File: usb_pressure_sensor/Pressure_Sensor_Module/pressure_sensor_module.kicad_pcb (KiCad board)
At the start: 2 copper layers, 3 parts, among them IC1 MS580314BA01-00, J1 MODULE_BRIDGE

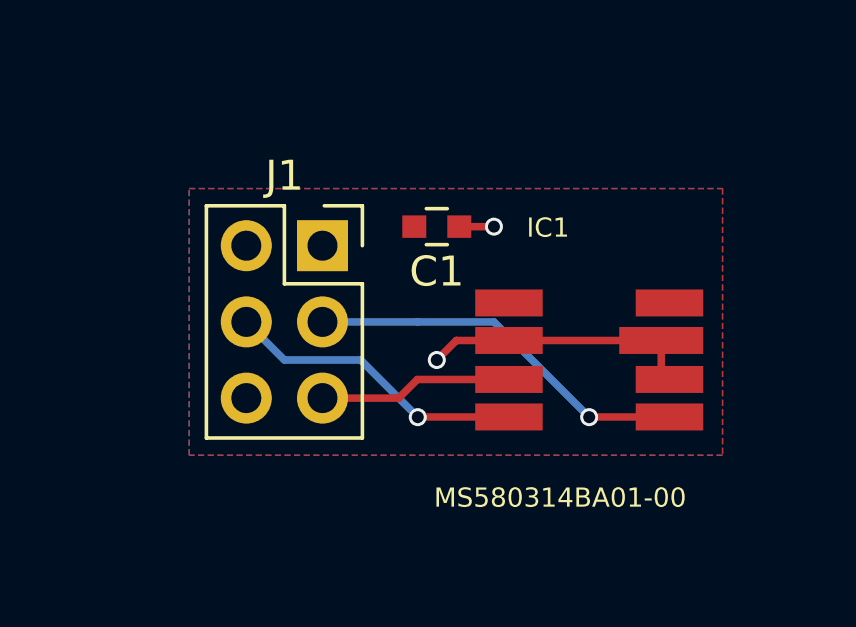
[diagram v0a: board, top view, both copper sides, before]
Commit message: PCB design with new pressure sensor and some footprints
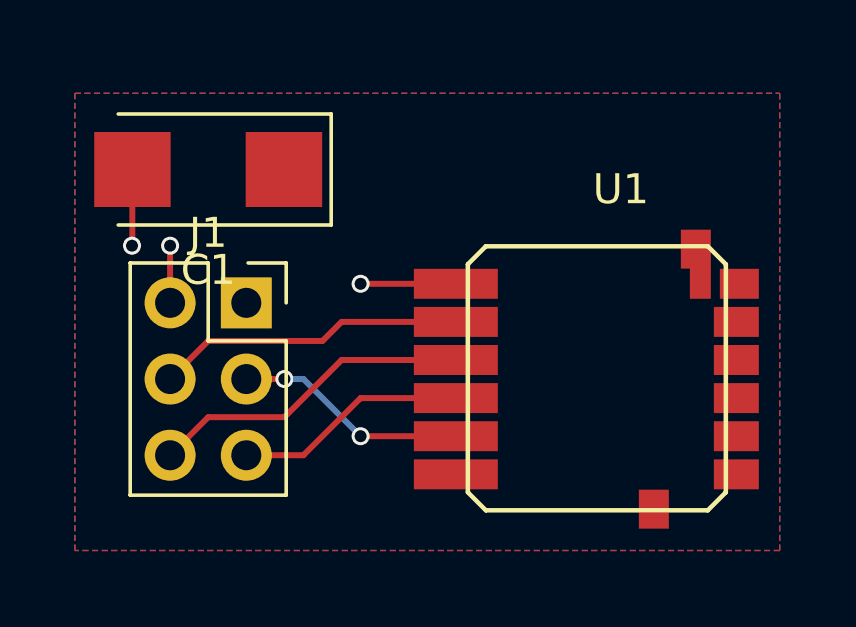
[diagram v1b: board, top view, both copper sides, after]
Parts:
- removed IC1: MS580314BA01-00, footprints:XDCR_MS580314BA01-00
- added U1: MS5535C, footprints:MS5535C, F.Cu at (144.1, 111.8)
- C1: value 100n -> 47u; footprint Capacitors_SMD:C_0603 -> Capacitors_Tantalum_SMD:CP_Tantalum_Case-C_EIA-6032-28_Reflow
- moved C1 7.85 mm to (135.9, 101.6)
- moved J1 3.17 mm to (137.2, 106.0)
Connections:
- C1 pad 1: /GND -> /3v3
- C1 pad 2: /VCC -> /GND
- J1 pad 1: /GND -> /3v3
- J1 pad 2: /VCC -> /GND
- J1 pad 3: /SPI_SCLK -> /MCLK
- J1 pad 4: /SPI_MISO -> /SCLK
- J1 pad 5: /SPI_MOSI -> /DIN
- J1 pad 6: Net-(J1-Pad6) -> /DOUT
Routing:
- net /SPI_SCLK: track 12.9 -> 0.00 mm, vias 1 -> 0
- net /DOUT: track 0.00 -> 10.8 mm
- net /SCLK: track 0.00 -> 10.3 mm
- net /SPI_MISO: track 10.1 -> 0.00 mm, vias 1 -> 0
- net /MCLK: track 0.00 -> 7.77 mm, vias 0 -> 2
- net /DIN: track 0.00 -> 7.77 mm
- net /SPI_MOSI: track 6.47 -> 0.00 mm
- net /GND: track 10.3 -> 7.63 mm, vias 2 -> 3
- added copper zone on F.Cu, net /3v3
- removed copper zone on F.Cu, net /VCC
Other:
- net class Default: trace_width 0.25 -> 0.2
- rule pad_to_mask_clearance: 0.2 -> 0

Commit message: added cuts and drills + logos into the PCBs
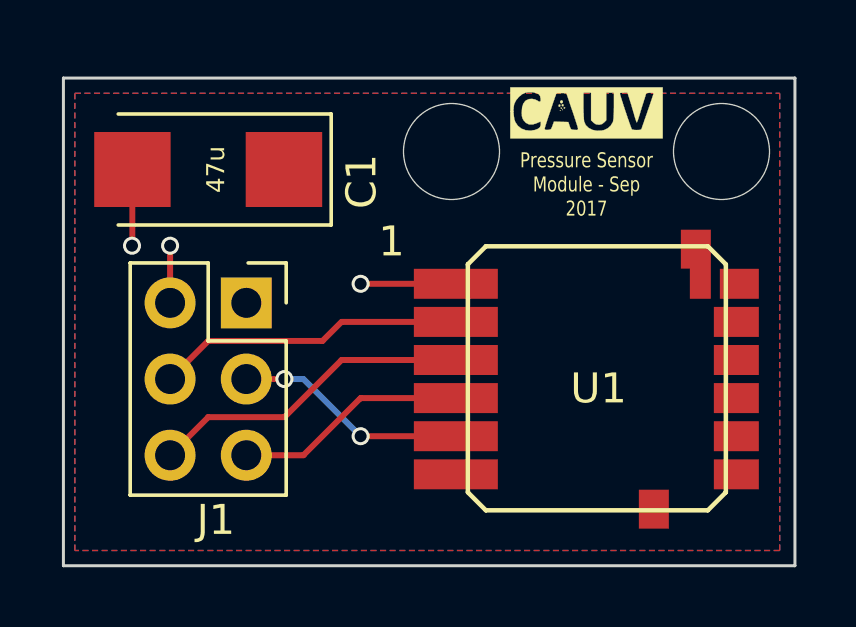
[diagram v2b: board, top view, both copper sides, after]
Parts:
- added G***: LOGO, footprints:LOGO, F.Cu at (148.5, 99.7)
- added REF**: M3_HOLE, agg:M3_HOLE, F.Cu at (144.0, 101.0)
- added REF**: M3_HOLE, agg:M3_HOLE, F.Cu at (153.0, 101.0)
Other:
- board outline added: 24.4 x 16.3 mm
- board text added: "1"
- board text added: "47u"
- board text added: "Pressure Sensor Module - Sep 2017"

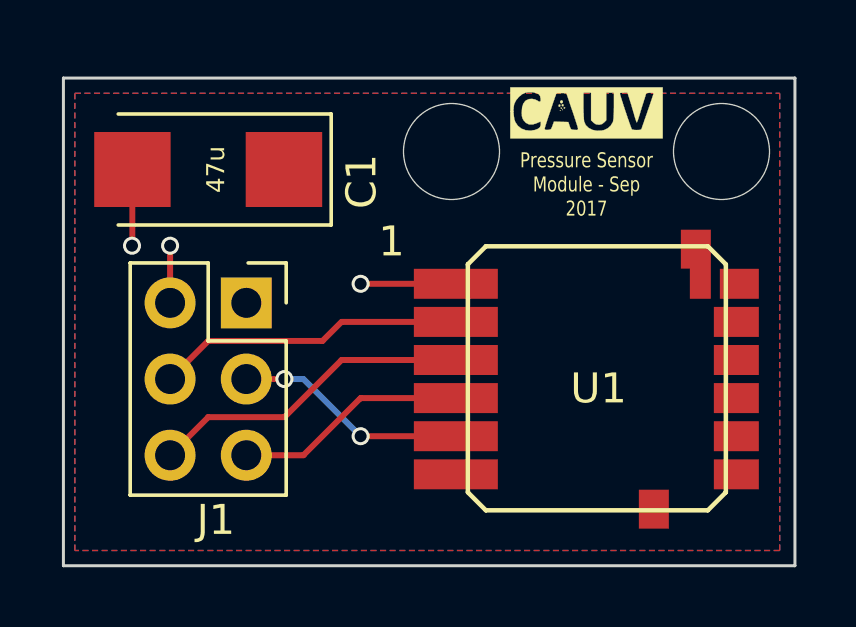
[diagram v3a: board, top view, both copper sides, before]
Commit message: removed unnecessary via
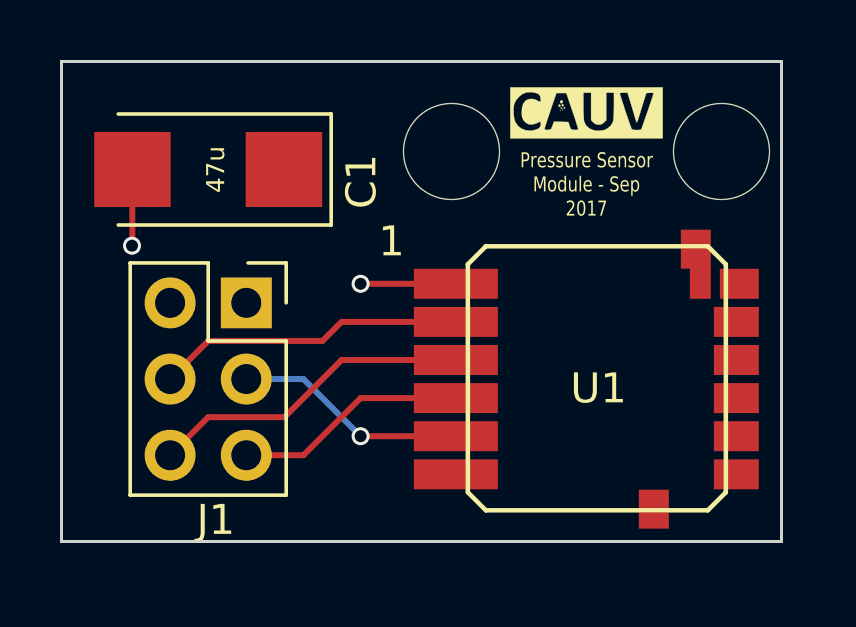
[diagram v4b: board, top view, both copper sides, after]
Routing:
- net /GND: track 7.63 -> 5.72 mm, vias 3 -> 2
- net /MCLK: vias 2 -> 1
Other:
- board size 24.4 x 16.3 mm -> 24 x 16 mm
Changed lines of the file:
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@@
     (thickness 1.6)
     (drawings 7)
-    (tracks 24)
+    (tracks 20)
     (zones 0)
     (modules 6)
@@
   (page A4)
   (layers
-    (0 F.Cu signal hide)
-    (31 B.Cu signal hide)
+    (0 F.Cu signal)
+    (31 B.Cu signal)
     (32 B.Adhes user hide)
     (33 F.Adhes user hide)
@@
     (pad "" np_thru_hole circle (at 0 0) (size 3.2 3.2) (drill 3.2) (layers *.Cu F.Mask))
   )
+  (module agg:M3_HOLE (layer F.Cu)
+    (at 153 101)
+    (fp_text reference REF** (at 0 -2.5) (layer F.Fab) hide
+      (effects (font (size 1 1) (thickness 0.15)))
+    )
+    (fp_text value M3_HOLE (at 0 2.5) (layer F.Fab) hide
+      (effects (font (size 1 1) (thickness 0.15)))
+    )
+    (fp_line (start -1.8 1.8) (end -1.8 -1.8) (layer F.CrtYd) (width 0.01))
+    (fp_line (start 1.8 1.8) (end -1.8 1.8) (layer F.CrtYd) (width 0.01))
+    (fp_line (start 1.8 -1.8) (end 1.8 1.8) (layer F.CrtYd) (width 0.01))
+    (fp_line (start -1.8 -1.8) (end 1.8 -1.8) (layer F.CrtYd) (width 0.01))
+    (pad "" np_thru_hole circle (at 0 0) (size 3.2 3.2) (drill 3.2) (layers *.Cu F.Mask))
+  )
   (module Capacitors_Tantalum_SMD:CP_Tantalum_Case-C_EIA-6032-28_Reflow (layer F.Cu)
     (at 135.89 101.6 180)
@@
     (pad 14 smd rect (at -8.15 6.3525 180) (size 0.7 1.005) (layers F.Cu F.Paste F.Mask))
     (pad 14 smd rect (at -8 7.505 180) (size 1 1.3) (layers F.Cu F.Paste F.Mask))
-  )
-  (module agg:M3_HOLE (layer F.Cu)
-    (at 153 101)
-    (fp_text reference REF** (at 0 -2.5) (layer F.Fab) hide
-      (effects (font (size 1 1) (thickness 0.15)))
-    )
-    (fp_text value M3_HOLE (at 0 2.5) (layer F.Fab) hide
-      (effects (font (size 1 1) (thickness 0.15)))
-    )
-    (fp_line (start -1.8 1.8) (end -1.8 -1.8) (layer F.CrtYd) (width 0.01))
-    (fp_line (start 1.8 1.8) (end -1.8 1.8) (layer F.CrtYd) (width 0.01))
-    (fp_line (start 1.8 -1.8) (end 1.8 1.8) (layer F.CrtYd) (width 0.01))
-    (fp_line (start -1.8 -1.8) (end 1.8 -1.8) (layer F.CrtYd) (width 0.01))
-    (pad "" np_thru_hole circle (at 0 0) (size 3.2 3.2) (drill 3.2) (layers *.Cu F.Mask))
   )
   (module footprints:LOGO (layer F.Cu)
@@
       (xy -0.794329 -0.385252)) (layer F.SilkS) (width 0.01))
   )
+  (gr_line (start 155 98) (end 155 114) (layer Edge.Cuts) (width 0.1))
+  (gr_line (start 131 98) (end 155 98) (layer Edge.Cuts) (width 0.1))
+  (gr_line (start 131 114) (end 131 98) (layer Edge.Cuts) (width 0.1))
+  (gr_line (start 155 114) (end 131 114) (layer Edge.Cuts) (width 0.1))
   (gr_text "Pressure Sensor\nModule - Sep\n2017" (at 148.5 102.1) (layer F.SilkS)
     (effects (font (size 0.5 0.4) (thickness 0.1)))
@@
     (effects (font (size 0.6 0.6) (thickness 0.15)))
   )
-  (gr_line (start 155.448 98.552) (end 131.064 98.552) (angle 90) (layer Edge.Cuts) (width 0.1))
-  (gr_line (start 155.448 114.808) (end 155.448 98.552) (angle 90) (layer Edge.Cuts) (width 0.1))
-  (gr_line (start 131.064 114.808) (end 155.448 114.808) (angle 90) (layer Edge.Cuts) (width 0.1))
-  (gr_line (start 131.064 98.552) (end 131.064 114.808) (angle 90) (layer Edge.Cuts) (width 0.1))
   (segment (start 144.145 105.41) (end 140.97 105.41) (width 0.2) (layer F.Cu) (net 2))
   (via (at 140.97 105.41) (size 0.6) (drill 0.4) (layers F.Cu B.Cu) (net 2))
-  (segment (start 134.62 106.045) (end 134.62 104.14) (width 0.2) (layer F.Cu) (net 2))
-  (via (at 134.62 104.14) (size 0.6) (drill 0.4) (layers F.Cu B.Cu) (net 2))
   (segment (start 133.365 101.6) (end 133.365 104.125) (width 0.2) (layer F.Cu) (net 2))
   (via (at 133.35 104.14) (size 0.6) (drill 0.4) (layers F.Cu B.Cu) (net 2))
   (segment (start 133.365 104.125) (end 133.35 104.14) (width 0.2) (layer F.Cu) (net 2))
+  (segment (start 139.065 108.585) (end 137.16 108.585) (width 0.2) (layer B.Cu) (net 3))
   (segment (start 144.145 110.49) (end 140.97 110.49) (width 0.2) (layer F.Cu) (net 3))
-  (segment (start 138.43 108.585) (end 137.16 108.585) (width 0.2) (layer F.Cu) (net 3))
-  (via (at 138.43 108.585) (size 0.6) (drill 0.4) (layers F.Cu B.Cu) (net 3))
-  (segment (start 139.065 108.585) (end 138.43 108.585) (width 0.2) (layer B.Cu) (net 3))
   (segment (start 140.97 110.49) (end 139.065 108.585) (width 0.2) (layer B.Cu) (net 3))
   (via (at 140.97 110.49) (size 0.6) (drill 0.4) (layers F.Cu B.Cu) (net 3))
@@
   (segment (start 138.43 109.855) (end 135.89 109.855) (width 0.2) (layer F.Cu) (net 6))
   (segment (start 140.335 107.95) (end 138.43 109.855) (width 0.2) (layer F.Cu) (net 6))
+  (zone (net 1) (net_name /3v3) (layer F.Cu) (hatch edge 0.508)
+    (connect_pads (clearance 0.508))
+    (min_thickness 0.254)
+    (fill yes (arc_segments 16) (thermal_gap 0.508) (thermal_bridge_width 0.508))
+    (polygon
+      (pts
+        (xy 131 98) (xy 131 114) (xy 155 114) (xy 155 98)
+      )
+    )
+  )
   (zone (net 2) (net_name /GND) (layer B.Cu) (hatch edge 0.508)
     (connect_pads (clearance 0.508))
@@
     (polygon
       (pts
-        (xy 154.94 114.3) (xy 131.445 114.3) (xy 131.445 99.06) (xy 154.94 99.06)
+        (xy 155 98) (xy 155 114) (xy 131 114) (xy 131 98)
       )
     )
-  )
-  (zone (net 1) (net_name /3v3) (layer F.Cu) (hatch edge 0.508)
-    (connect_pads (clearance 0.508))
-    (min_thickness 0.254)
-    (fill yes (arc_segments 16) (thermal_gap 0.508) (thermal_bridge_width 0.508))
-    (polygon
-      (pts
-        (xy 154.94 114.3) (xy 131.445 114.3) (xy 131.445 99.06) (xy 154.94 99.06)
-      )
-    )
